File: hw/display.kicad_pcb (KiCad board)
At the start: 2 copper layers, 100 x 40.1 mm, 53 parts, among them J101 AMPSEAL_8_POS_VERT_BLACK_SEAL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, J301 HEADER_MOLEX_54104-4031, J302 HEADER_MOLEX_52207-0433, J401 ARM_JTAG_SWD_HEADER_10_PINSMD, U101 MCP2551_SOIC8, U301 FT812, U302 AL8805W5-7_LED_DRIVER, U401 LPC1549JBD64, U501 WINDBOND_W25Q128JVSIQ_SOIC8_W, U601 OPAMP_LM358DT, U701 RTC_S-35390A-J8T1G, X401 XTAL_7A-12.000MAAJ-T, X601 BUZZER_PKM13EPYH4002-B0, X701 XTAL_ABS25-32.768KHZ-T

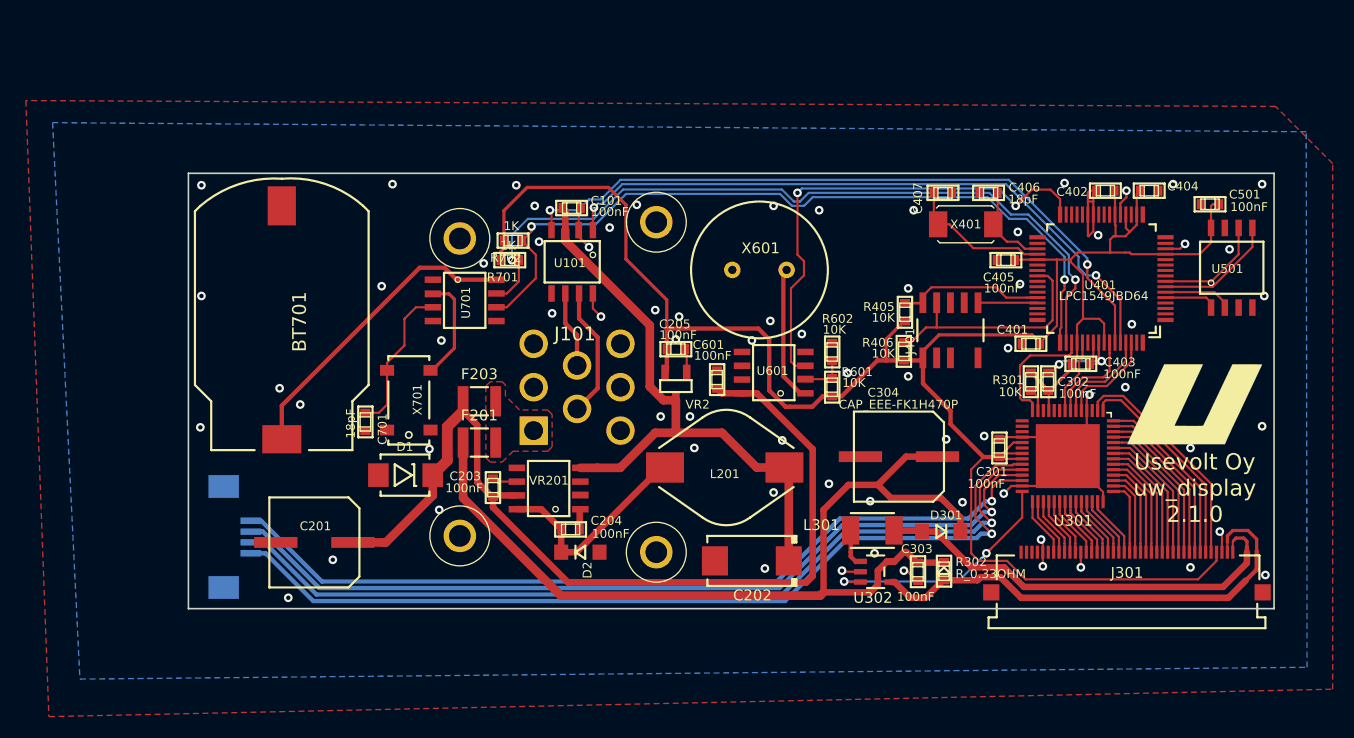
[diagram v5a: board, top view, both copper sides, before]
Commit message: displa pcb reverted back to 1.6.0 revision and imporved to 1.7.0
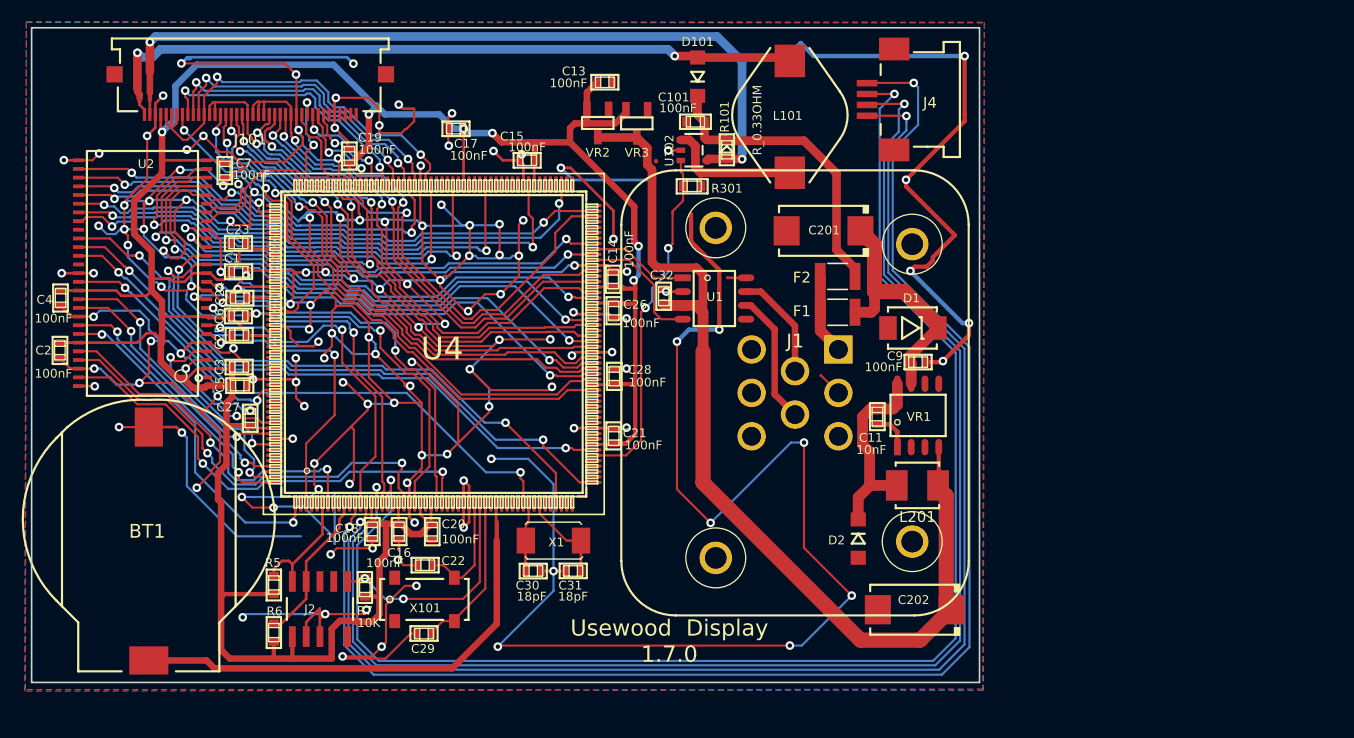
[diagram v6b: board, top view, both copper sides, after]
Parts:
- removed BT701: BATTERY_HOLDER_CH7410-2032LFSMD, usevolt:BATTERY_HOLDER_CH7410-2032LF
- removed C203, C204, C205, C301, C302, C303, C401, C402, C403, C404, C405, C501, C601: 100nF, kemet:0603
- removed C304: CAP_EEE-FK1H470P, usevolt:CAP_EEE-FK1H470P
- removed C406, C407, C701: 18pF, kemet:0603
- removed D301: DIODE_RS07J-GS18, usevolt:DO219AB
- removed F201, F203: FUSE_0ZCH0075AF2E, usevolt:1210
- removed G***: LOGO, usevolt:uv_logo
- removed J301: HEADER_MOLEX_54104-4031, usevolt:HEADER_MOLEX_54104-4031
- removed J302: HEADER_MOLEX_52207-0433, usevolt:HEADER_MOLEX_52207-0433
- removed J401: ARM_JTAG_SWD_HEADER_10_PINSMD, usevolt:ARM_10_PIN_JTAG_SWD_CONNECTOR
- removed L301: IND_744045210, usevolt:IND_744045210
- removed R302: R_0.33OHM, usevolt:0603
- removed R405, R406, R601, R602: 10K, multicomp:0603
- removed R701, R702: 1K, yageo:0603
- removed U101: MCP2551_SOIC8, usevolt:SOIC8
- removed U301: FT812, usevolt:QFN-56
- removed U302: AL8805W5-7_LED_DRIVER, usevolt:SOT-25
- removed U401: LPC1549JBD64, usevolt:QFP64
- removed U501: WINDBOND_W25Q128JVSIQ_SOIC8_W, usevolt:SOIC8_W
- removed U601: OPAMP_LM358DT, usevolt:SOIC8
- removed U701: RTC_S-35390A-J8T1G, usevolt:SOIC8
- removed VR201: LM2671SOIC8, usevolt:SOIC8
- removed X401: XTAL_7A-12.000MAAJ-T, usevolt:XTAL_7A-20.000MAJ
- removed X601: BUZZER_PKM13EPYH4002-B0, usevolt:BUZZER_PKM13EPYH4002-B0
- removed X701: XTAL_ABS25-32.768KHZ-T, usevolt:XTAL_32.768KHZ-T
- added BT1: BATTERY_HOLDER_CH7410-2032LFSMD, usevolt:usevolt-BATTERY_HOLDER_CH7410-2032LF, F.Cu at (98.6, 93.7)
- added C1: 100nF, kemet:Kemet-CAPC1608X85N, F.Cu at (106.8, 79.4)
- added C11: 10nF, kemet:Kemet-CAPC1608X85N, F.Cu at (165.7, 92.7)
- added C13: 100nF, kemet:Kemet-CAPC1608X85N, F.Cu at (140.6, 61.9)
- added C14: 100nF, kemet:Kemet-CAPC1608X85N, F.Cu at (141.3, 80.1)
- added C15: 100nF, kemet:Kemet-CAPC1608X85N, F.Cu at (133.4, 69.1)
- added C16: 100nF, kemet:Kemet-CAPC1608X85N, F.Cu at (121.6, 103.3)
- added C17: 100nF, kemet:Kemet-CAPC1608X85N, F.Cu at (126.8, 66.2)
- added C18: 100nF, kemet:Kemet-CAPC1608X85N, F.Cu at (119.1, 103.3)
- added C19: 100nF, kemet:Kemet-CAPC1608X85N, F.Cu at (117.0, 68.7)
- added C2: 100nF, kemet:Kemet-CAPC1608X85N, F.Cu at (90.4, 86.6)
- added C20: 100nF, kemet:Kemet-CAPC1608X85N, F.Cu at (124.7, 103.3)
- added C21: 100nF, kemet:Kemet-CAPC1608X85N, F.Cu at (141.4, 94.5)
- added C22: 12pF, kemet:Kemet-CAPC1608X85N, F.Cu at (124.0, 106.4)
- added C23: 100nF, kemet:Kemet-CAPC1608X85N, F.Cu at (106.8, 76.8)
- added C24: 100nF, kemet:Kemet-CAPC1608X85N, F.Cu at (106.9, 81.8)
- added C25: 100nF, kemet:Kemet-CAPC1608X85N, F.Cu at (106.9, 85.2)
- added C26: 100nF, kemet:Kemet-CAPC1608X85N, F.Cu at (141.4, 83.0)
- added C27: 100nF, kemet:Kemet-CAPC1608X85N, F.Cu at (107.9, 92.9)
- added C28: 100nF, kemet:Kemet-CAPC1608X85N, F.Cu at (141.4, 89.0)
- added C29: 12pF, kemet:Kemet-CAPC1608X85N, F.Cu at (123.9, 112.7)
- added C3: 100nF, kemet:Kemet-CAPC1608X85N, F.Cu at (106.9, 88.1)
- added C30: 18pF, kemet:Kemet-CAPC1608X85N, F.Cu at (134.0, 106.9)
- added C31: 18pF, kemet:Kemet-CAPC1608X85N, F.Cu at (137.6, 106.9)
- added C32: 100nF, kemet:Kemet-CAPC1608X85N, F.Cu at (146.0, 81.6)
- added C4: 100nF, kemet:Kemet-CAPC1608X85N, F.Cu at (90.4, 81.8)
- added C5: 100nF, kemet:Kemet-CAPC1608X85N, F.Cu at (106.9, 89.9)
- added C6: 100nF, kemet:Kemet-CAPC1608X85N, F.Cu at (106.8, 83.4)
- added C7: 100nF, kemet:Kemet-CAPC1608X85N, F.Cu at (105.6, 70.1)
- added C9: 100nF, kemet:Kemet-CAPC1608X85N, F.Cu at (169.4, 87.7)
- added D101: DIODE_RS07J-GS18, usevolt:DO219AB, F.Cu at (149.1, 61.4)
- added F1: FUSE_0ZCH0075AF2E, usevolt:1210, F.Cu at (162.0, 83.1)
- added F2: FUSE_0ZCH0075AF2E, usevolt:1210, F.Cu at (162.0, 79.8)
- added J1: AMPSEAL_8_POS_776275-1, usevolt:AMPSEAL_8_POS_776275-1, F.Cu at (158.1, 90.5)
- added J2: ARM_JTAG_SWD_HEADER_10_PINSMD, usevolt:usevolt-ARM_10_PIN_JTAG_SWD_CONNECTOR, F.Cu at (111.8, 111.7)
- added J4: HEADER_MOLEX_52207-0433, usevolt:HEADER_MOLEX_52207-0433, F.Cu at (169.1, 63.5)
- added L101: INDUCTOR_SDR1005-101KL, usevolt:INDUCTOR_BOURNS_10X13X5MM, F.Cu at (157.6, 65.1)
- added R101: R_0.33OHM, usevolt:0603, F.Cu at (151.8, 68.1)
- added R5: 10K, multicomp:Multicomp-RESC1608X60N, F.Cu at (110.1, 108.2)
- added R6: 10K, multicomp:Multicomp-RESC1608X60N, F.Cu at (110.1, 112.6)
- added R7: 10K, multicomp:Multicomp-RESC1608X60N, F.Cu at (118.5, 108.5)
- added U1: MCP2551_SOIC8, usevolt:SOIC8, F.Cu at (150.6, 81.8)
- added U102: AL8805W5-7_LED_DRIVER, usevolt:SOT-25, F.Cu at (148.8, 68.2)
- added U2: ALLIANCE_AS4C4M16SA_TSOP_II, usevolt:TSOP_II_54_PIN, F.Cu at (98.0, 79.5)
- added U4: LPC1785FBD208_551QFP50, usevolt:QFP208, F.Cu at (124.8, 86.0)
- added VR1: LM2671SOIC8, usevolt:SOIC8, F.Cu at (169.4, 92.6)
- added VR3: REG_MCP1700, usevolt:SOT-23_3-PIN, F.Cu at (143.5, 65.7)
- added X1: XTAL_7A-20.000MAAJ-T, usevolt:XTAL_7A-20.000MAJ, F.Cu at (135.8, 104.1)
- added X101: XTAL_ABS25-32.768KHZ-T, usevolt:XTAL_32.768KHZ-T, F.Cu at (124.0, 109.5)
- C201: value CAP_EEE-FK1H470P -> T491D226K035AT; footprint usevolt:CAP_EEE-FK1H470P -> kemet:7343
- J101: value AMPSEAL_8_POS_VERT_BLACK_SEALED_1-776276-1 -> HEADER_MOLEX_54104-4031; footprint usevolt:AMPSEAL_8_POS_776275-1 -> usevolt:HEADER_MOLEX_54104-4031
- L201: value INDUCTOR_SDR1005-101KL -> IND_744045210; footprint usevolt:INDUCTOR_BOURNS_10X13X5MM -> usevolt:IND_744045210
- moved C201 55.0 mm to (160.7, 75.6), turned to 180 degrees
- moved D1 48.7 mm to (168.9, 84.5)
- moved J101 40.9 mm to (107.9, 62.4), turned to 180 degrees
- moved R301 36.0 mm to (148.6, 71.5), turned to 180 degrees
- moved D2 25.6 mm to (163.9, 104.0), turned to 90 degrees
- moved VR2 25.3 mm to (139.9, 65.7)
- moved L201 17.8 mm to (169.3, 99.0)
- moved C202 15.7 mm to (169.1, 110.5)
- moved C101 13.9 mm to (148.9, 65.5)
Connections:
- C101 pad 1: +5V -> GND
- C101 pad 2: GND -> /pwr_supply_sheet/VLCD
- D2 pad P$2: Net-(C204-Pad2) -> Net-(C11-Pad2)
- J101 pad 1: /power_supply/VIN -> /BCKL-
- J101 pad 10: (no net) -> /R2
- J101 pad 11: (no net) -> /R3
- J101 pad 12: (no net) -> /R4
- J101 pad 2: GND -> /BCKL+
- J101 pad 3: (no net) -> GND
- J101 pad 4: /CANH -> +3V3
- J101 pad 5: /CANL -> /R4
- J101 pad 6: (no net) -> /R4
- J101 pad 7: (no net) -> /R4
- J101 pad 8: (no net) -> /R0
- J101 pad 9: (no net) -> /R1
- R301 pad 1: Net-(R301-Pad1) -> GND
- R301 pad 2: +3V3 -> /BACKLIGHT
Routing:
- net GND: track 72.7 -> 884.8 mm, vias 72 -> 143
- net /lpc1785_sheet/LCD_Y_T: track 0.00 -> 133.6 mm, vias 0 -> 2
- net /lpc1785_sheet/LCD_X_R: track 0.00 -> 131.2 mm, vias 0 -> 2
- net /lpc1785_sheet/LCD_Y_B: track 0.00 -> 131.0 mm, vias 0 -> 2
- net /lpc1785_sheet/LCD_X_L: track 0.00 -> 128.1 mm, vias 0 -> 2
- net +3V3: track 203.7 -> 295.0 mm, vias 0 -> 6
- net VEE: track 86.3 -> 0.00 mm
- net /TFT-LCD/XL: track 82.8 -> 0.00 mm, vias 1 -> 0
- net /TFT-LCD/YD: track 81.3 -> 0.00 mm, vias 1 -> 0
- net /TFT-LCD/XR: track 79.9 -> 0.00 mm, vias 1 -> 0
- net /TFT-LCD/YU: track 77.9 -> 0.00 mm, vias 1 -> 0
- net /BCKL+: track 0.00 -> 74.7 mm, vias 0 -> 2
- net /lpc1549/RTC_SDA: track 72.3 -> 0.00 mm, vias 2 -> 0
- net /lpc1549/RTC_SCL: track 71.9 -> 0.00 mm, vias 2 -> 0
- net /BCKL-: track 0.00 -> 67.0 mm, vias 0 -> 2
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- removed copper zone on F.Cu, net /power_supply/VIN
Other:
- board size 100 x 40.1 mm -> 87.3 x 60.3 mm
- rule trace_min: 0 -> 0.2
- board text added: "Usewood Display 1.7.0"
- board text removed: "Usevolt Oy uw_display 2.1.0"
